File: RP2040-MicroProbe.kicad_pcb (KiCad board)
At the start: 4 copper layers, 39.4 x 17.8 mm, 47 parts, among them J1 CONN_MCU_DEBUG, J2 CONN_DBG_COMB, J5 USB_B_Micro, J7 CONN_DBG_JTAG, U1 W25Q128JVS, U2 RP2040, U3 74AUP1T17, U4 W25Q128JVEIQ, U5 MIC5205-3.3YM5, U6 74AUP1T17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

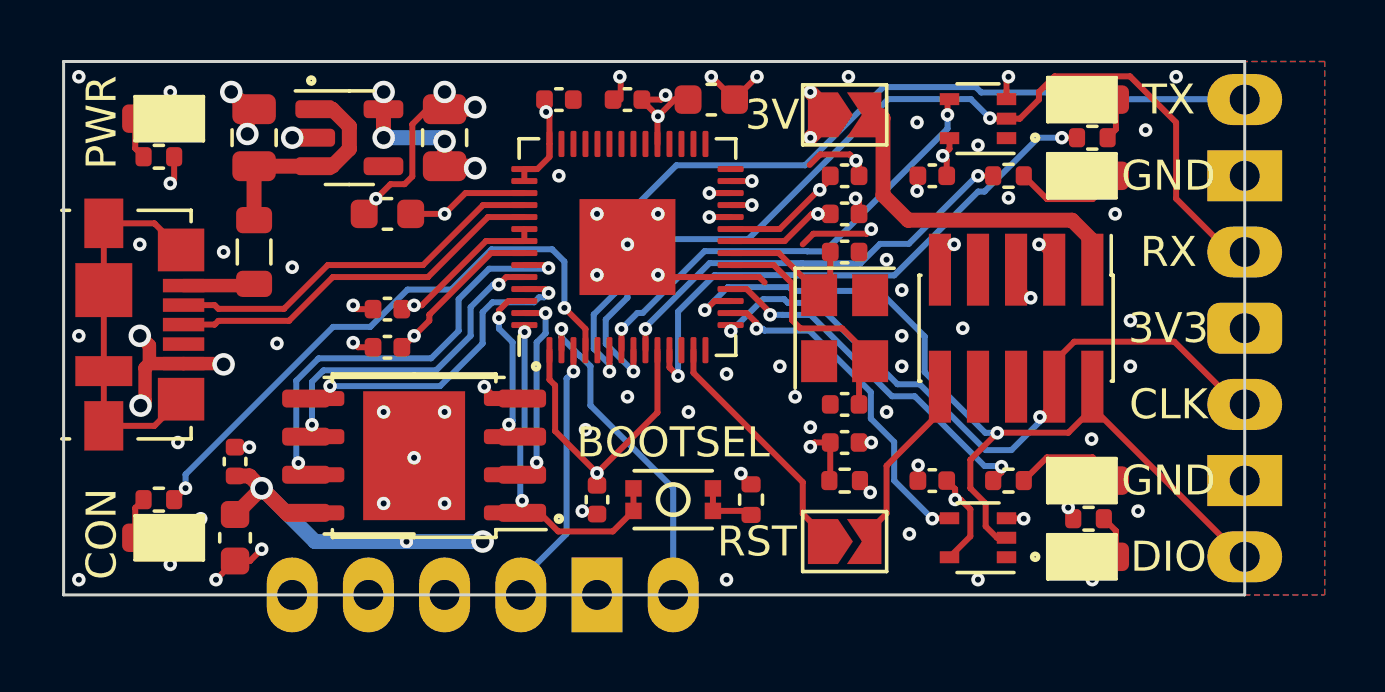
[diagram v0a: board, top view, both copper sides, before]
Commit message: Rotated JTAG connector. Moved stuff around
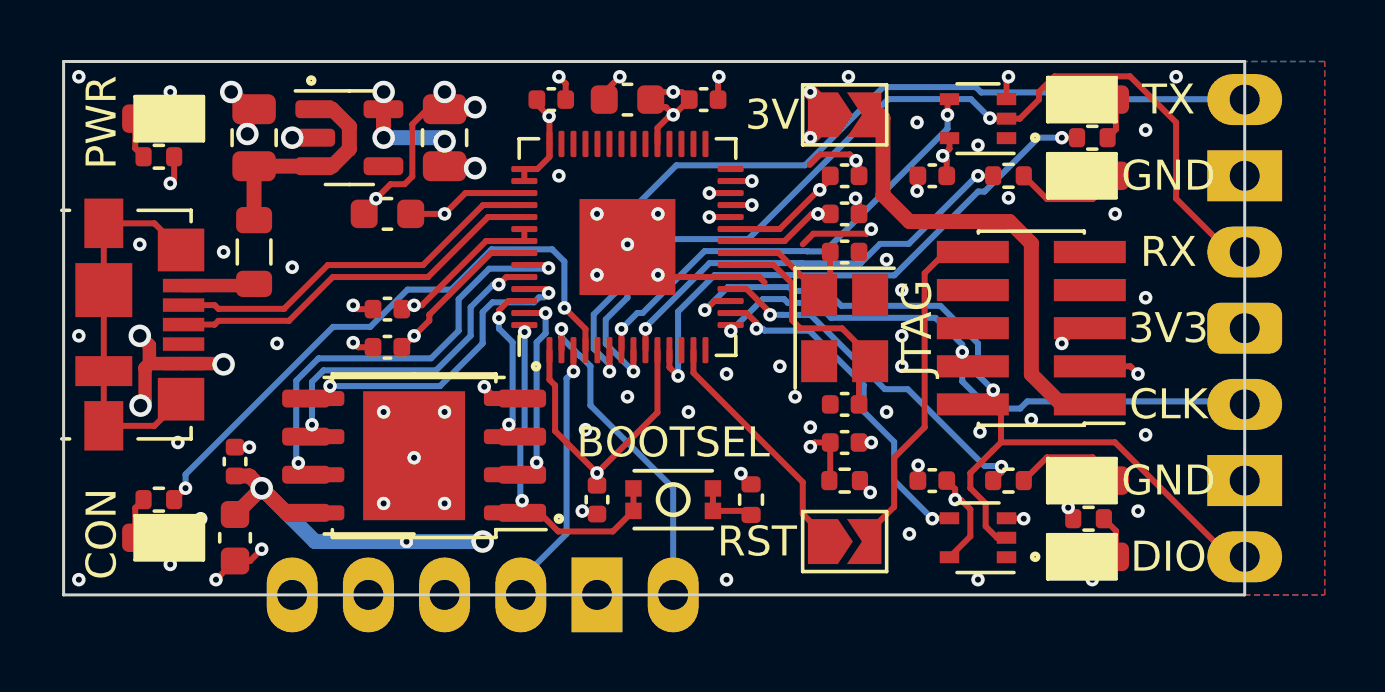
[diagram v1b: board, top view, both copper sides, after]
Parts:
- moved C1 2.79 mm to (145.8, 93.7), turned to 180 degrees
- moved C4 2.54 mm to (148.3, 93.7), turned to 0 degrees
- moved J7 0.51 mm to (159.3, 101.3), turned to 180 degrees
- moved C6 0.25 mm to (143.3, 93.7)
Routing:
- net TARGET_RESET: track 6.05 -> 11.6 mm
- net TARGET_3V3: track 11.7 -> 15.5 mm
- net DBG_CLK: track 23.0 -> 20.8 mm
- net GND: track 44.1 -> 43.4 mm, vias 84 -> 83
- net DBG_DIO: track 30.3 -> 29.7 mm
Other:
- board text added: "JTAG"
